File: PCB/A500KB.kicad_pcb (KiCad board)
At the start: 2 copper layers, 448.4 x 139.2 mm, 224 parts, among them J1 Conn_01x31, J2 USB_B, J3 Conn_02x03_Odd_Even, J4 Conn_01x08_Male, J5 Conn_01x02, Q1 MMBT3904, U1 IS32FL3237_DS, U2 AT90USB1287-AU, Y2 16 MHz

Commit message: added Spacebar holder for extra springs, adjusted PCB
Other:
- board size 448.4 x 139.2 mm -> 447.8 x 139.2 mm

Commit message: PCB update, Amiga software update  - finished intended feature set for Amiga    software: auto-load from keyboard, some    status and error requesters, automatic    custom screen if there are not enough    available pens on Workbench
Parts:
- D10, D11, D12, D13, D14, D15, D16, D17, D18, D19, D20, D21, D22, D23, D24, D25, D26, D27, D28, D29, D30, D31, D32, D33, D34, D35, D36, D37, D38, D39, D40, D41, D42, D43, D44, D45, D46, D47, D48, D49, D50, D54, D55, D56, D57, D58, D59, D60, D61, D62, D63, D64, D65, D66, D67, D68, D8, D9: value 1N914WT -> 1N4148W; footprint Diode_SMD:D_SOD-523 -> Diode_SMD:D_SOD-123
- moved D54 1.31 mm to (54.6, 267.5), turned to 270 degrees
- moved D36 1.25 mm to (296.8, 305.8), turned to 270 degrees
- moved D20 1.19 mm to (387.8, 324.6), turned to 270 degrees
- moved D34 1.16 mm to (258.8, 305.7), turned to 270 degrees
- moved D28 1.16 mm to (144.3, 305.7), turned to 270 degrees
- moved D29 1.16 mm to (163.4, 305.7), turned to 270 degrees
- moved D31 1.16 mm to (201.5, 305.7), turned to 270 degrees
- moved D33 1.16 mm to (239.7, 305.7), turned to 270 degrees
- moved D35 1.16 mm to (277.8, 305.7), turned to 270 degrees
- moved D27 1.16 mm to (125.3, 305.7), turned to 270 degrees
- moved D26 1.15 mm to (106.2, 305.7), turned to 270 degrees
- moved D30 1.15 mm to (182.4, 305.7), turned to 270 degrees
- moved D25 1.15 mm to (87.1, 305.7), turned to 270 degrees
- moved D32 1.15 mm to (220.6, 305.7), turned to 270 degrees
- moved D9 1.12 mm to (96.6, 324.6), turned to 270 degrees
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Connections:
- D10 pad 1: Net-(D10-Pad1) -> /X6=3
- D10 pad 2: /X6=3 -> Net-(D10-Pad2)
- D11 pad 1: Net-(D11-Pad1) -> /X6=3
- D11 pad 2: /X6=3 -> Net-(D11-Pad2)
- D12 pad 1: Net-(D12-Pad1) -> /X6=3
- D12 pad 2: /X6=3 -> Net-(D12-Pad2)
- D13 pad 1: Net-(D13-Pad1) -> /X6=3
- D13 pad 2: /X6=3 -> Net-(D13-Pad2)
- D14 pad 1: Net-(D14-Pad1) -> /X6=3
- D14 pad 2: /X6=3 -> Net-(D14-Pad2)
- D15 pad 1: Net-(D15-Pad1) -> /X6=3
- D15 pad 2: /X6=3 -> Net-(D15-Pad2)
- D16 pad 1: Net-(D16-Pad1) -> /X6=3
- D16 pad 2: /X6=3 -> Net-(D16-Pad2)
- D17 pad 1: Net-(D17-Pad1) -> /X6=3
- D17 pad 2: /X6=3 -> Net-(D17-Pad2)
- D18 pad 1: Net-(D18-Pad1) -> /X6=3
- D18 pad 2: /X6=3 -> Net-(D18-Pad2)
- D19 pad 1: Net-(D19-Pad1) -> /X6=3
- D19 pad 2: /X6=3 -> Net-(D19-Pad2)
- D20 pad 1: Net-(D20-Pad1) -> /X5=2
- D20 pad 2: /X5=2 -> Net-(D20-Pad2)
- D21 pad 1: Net-(D21-Pad1) -> /X4=1
- D21 pad 2: /X4=1 -> Net-(D21-Pad2)
- D22 pad 1: Net-(D22-Pad1) -> /X3=5
- D22 pad 2: /X3=5 -> Net-(D22-Pad2)
- D23 pad 1: Net-(D23-Pad1) -> /X6=3
- D23 pad 2: /X6=3 -> Net-(D23-Pad2)
- D24 pad 1: Net-(D24-Pad1) -> /X5=2
- D24 pad 2: /X5=2 -> Net-(D24-Pad2)
- D25 pad 1: Net-(D25-Pad1) -> /X5=2
- D25 pad 2: /X5=2 -> Net-(D25-Pad2)
- D26 pad 1: Net-(D26-Pad1) -> /X5=2
- D26 pad 2: /X5=2 -> Net-(D26-Pad2)
- D27 pad 1: Net-(D27-Pad1) -> /X5=2
- D27 pad 2: /X5=2 -> Net-(D27-Pad2)
- D28 pad 1: Net-(D28-Pad1) -> /X5=2
- D28 pad 2: /X5=2 -> Net-(D28-Pad2)
- D29 pad 1: Net-(D29-Pad1) -> /X5=2
- D29 pad 2: /X5=2 -> Net-(D29-Pad2)
- D30 pad 1: Net-(D30-Pad1) -> /X5=2
- D30 pad 2: /X5=2 -> Net-(D30-Pad2)
- D31 pad 1: Net-(D31-Pad1) -> /X5=2
- D31 pad 2: /X5=2 -> Net-(D31-Pad2)
- D32 pad 1: Net-(D32-Pad1) -> /X5=2
- D32 pad 2: /X5=2 -> Net-(D32-Pad2)
- D33 pad 1: Net-(D33-Pad1) -> /X5=2
- D33 pad 2: /X5=2 -> Net-(D33-Pad2)
- D34 pad 1: Net-(D34-Pad1) -> /X5=2
- D34 pad 2: /X5=2 -> Net-(D34-Pad2)
- D35 pad 1: Net-(D35-Pad1) -> /X5=2
- D35 pad 2: /X5=2 -> Net-(D35-Pad2)
- D36 pad 1: Net-(D36-Pad1) -> /X5=2
- D36 pad 2: /X5=2 -> Net-(D36-Pad2)
- D37 pad 1: Net-(D37-Pad1) -> /X4=1
- D37 pad 2: /X4=1 -> Net-(D37-Pad2)
- D38 pad 1: Net-(D38-Pad1) -> /X4=1
- D38 pad 2: /X4=1 -> Net-(D38-Pad2)
- D39 pad 1: Net-(D39-Pad1) -> /X4=1
- D39 pad 2: /X4=1 -> Net-(D39-Pad2)
- D40 pad 1: Net-(D40-Pad1) -> /X4=1
- D40 pad 2: /X4=1 -> Net-(D40-Pad2)
- D41 pad 1: Net-(D41-Pad1) -> /X4=1
- D41 pad 2: /X4=1 -> Net-(D41-Pad2)
- D42 pad 1: Net-(D42-Pad1) -> /X4=1
- D42 pad 2: /X4=1 -> Net-(D42-Pad2)
- D43 pad 1: Net-(D43-Pad1) -> /X4=1
- D43 pad 2: /X4=1 -> Net-(D43-Pad2)
- D44 pad 1: Net-(D44-Pad1) -> /X4=1
- D44 pad 2: /X4=1 -> Net-(D44-Pad2)
- D45 pad 1: Net-(D45-Pad1) -> /X4=1
- D45 pad 2: /X4=1 -> Net-(D45-Pad2)
- D46 pad 1: Net-(D46-Pad1) -> /X4=1
- D46 pad 2: /X4=1 -> Net-(D46-Pad2)
- D47 pad 1: Net-(D47-Pad1) -> /X4=1
- D47 pad 2: /X4=1 -> Net-(D47-Pad2)
- D48 pad 1: Net-(D48-Pad1) -> /X4=1
- D48 pad 2: /X4=1 -> Net-(D48-Pad2)
- D49 pad 1: Net-(D49-Pad1) -> /X4=1
- D49 pad 2: /X4=1 -> Net-(D49-Pad2)
- D50 pad 1: Net-(D50-Pad1) -> /X4=1
- D50 pad 2: /X4=1 -> Net-(D50-Pad2)
- D54 pad 1: Net-(D54-Pad1) -> /X3=5
- D54 pad 2: /X3=5 -> Net-(D54-Pad2)
- D55 pad 1: Net-(D55-Pad1) -> /X3=5
- D55 pad 2: /X3=5 -> Net-(D55-Pad2)
- D56 pad 1: Net-(D56-Pad1) -> /X3=5
- D56 pad 2: /X3=5 -> Net-(D56-Pad2)
- D57 pad 1: Net-(D57-Pad1) -> /X3=5
- D57 pad 2: /X3=5 -> Net-(D57-Pad2)
- D58 pad 1: Net-(D58-Pad1) -> /X3=5
- D58 pad 2: /X3=5 -> Net-(D58-Pad2)
- D59 pad 1: Net-(D59-Pad1) -> /X3=5
- D59 pad 2: /X3=5 -> Net-(D59-Pad2)
- D60 pad 1: Net-(D60-Pad1) -> /X3=5
- D60 pad 2: /X3=5 -> Net-(D60-Pad2)
- D61 pad 1: Net-(D61-Pad1) -> /X3=5
- D61 pad 2: /X3=5 -> Net-(D61-Pad2)
- D62 pad 1: Net-(D62-Pad1) -> /X3=5
- D62 pad 2: /X3=5 -> Net-(D62-Pad2)
- D63 pad 1: Net-(D63-Pad1) -> /X3=5
- D63 pad 2: /X3=5 -> Net-(D63-Pad2)
- D64 pad 1: Net-(D64-Pad1) -> /X3=5
- D64 pad 2: /X3=5 -> Net-(D64-Pad2)
- D65 pad 1: Net-(D65-Pad1) -> /X3=5
- D65 pad 2: /X3=5 -> Net-(D65-Pad2)
- D66 pad 1: Net-(D66-Pad1) -> /X3=5
- D66 pad 2: /X3=5 -> Net-(D66-Pad2)
- D67 pad 1: Net-(D67-Pad1) -> /X3=5
- D67 pad 2: /X3=5 -> Net-(D67-Pad2)
- D68 pad 1: Net-(D68-Pad1) -> /X6=3
- D68 pad 2: /X6=3 -> Net-(D68-Pad2)
- D8 pad 1: Net-(D8-Pad1) -> /X6=3
- D8 pad 2: /X6=3 -> Net-(D8-Pad2)
- D9 pad 1: Net-(D9-Pad1) -> /X6=3
- D9 pad 2: /X6=3 -> Net-(D9-Pad2)
- MX10 pad 2: Net-(D24-Pad1) -> Net-(D24-Pad2)
- MX11 pad 2: Net-(D8-Pad1) -> Net-(D8-Pad2)
- MX14 pad 2: Net-(D56-Pad1) -> Net-(D56-Pad2)
- MX15 pad 2: Net-(D39-Pad1) -> Net-(D39-Pad2)
- MX16 pad 2: Net-(D25-Pad1) -> Net-(D25-Pad2)
- MX17 pad 2: Net-(D9-Pad1) -> Net-(D9-Pad2)
- MX19 pad 2: Net-(D57-Pad1) -> Net-(D57-Pad2)
- MX2 pad 2: Net-(D54-Pad1) -> Net-(D54-Pad2)
- MX20 pad 2: Net-(D40-Pad1) -> Net-(D40-Pad2)
- MX21 pad 2: Net-(D26-Pad1) -> Net-(D26-Pad2)
- MX22 pad 2: Net-(D10-Pad1) -> Net-(D10-Pad2)
- MX24 pad 2: Net-(D58-Pad1) -> Net-(D58-Pad2)
- MX25 pad 2: Net-(D41-Pad1) -> Net-(D41-Pad2)
- MX26 pad 2: Net-(D27-Pad1) -> Net-(D27-Pad2)
- MX27 pad 2: Net-(D11-Pad1) -> Net-(D11-Pad2)
- MX29 pad 2: Net-(D59-Pad1) -> Net-(D59-Pad2)
- MX3 pad 2: Net-(D37-Pad1) -> Net-(D37-Pad2)
- MX30 pad 2: Net-(D42-Pad1) -> Net-(D42-Pad2)
- MX31 pad 2: Net-(D28-Pad1) -> Net-(D28-Pad2)
- MX32 pad 2: Net-(D12-Pad1) -> Net-(D12-Pad2)
- MX33 pad 2: Net-(D13-Pad1) -> Net-(D13-Pad2)
- MX35 pad 2: Net-(D60-Pad1) -> Net-(D60-Pad2)
- MX36 pad 2: Net-(D43-Pad1) -> Net-(D43-Pad2)
- MX37 pad 2: Net-(D29-Pad1) -> Net-(D29-Pad2)
- MX38 pad 2: Net-(D14-Pad1) -> Net-(D14-Pad2)
- MX40 pad 2: Net-(D61-Pad1) -> Net-(D61-Pad2)
- MX41 pad 2: Net-(D44-Pad1) -> Net-(D44-Pad2)
- MX42 pad 2: Net-(D30-Pad1) -> Net-(D30-Pad2)
- MX43 pad 2: Net-(D15-Pad1) -> Net-(D15-Pad2)
- MX45 pad 2: Net-(D62-Pad1) -> Net-(D62-Pad2)
- MX46 pad 2: Net-(D45-Pad1) -> Net-(D45-Pad2)
- MX47 pad 2: Net-(D31-Pad1) -> Net-(D31-Pad2)
- MX48 pad 2: Net-(D16-Pad1) -> Net-(D16-Pad2)
- MX50 pad 2: Net-(D63-Pad1) -> Net-(D63-Pad2)
- MX51 pad 2: Net-(D46-Pad1) -> Net-(D46-Pad2)
- MX52 pad 2: Net-(D32-Pad1) -> Net-(D32-Pad2)
- MX53 pad 2: Net-(D17-Pad1) -> Net-(D17-Pad2)
- MX55 pad 2: Net-(D64-Pad1) -> Net-(D64-Pad2)
- MX56 pad 2: Net-(D47-Pad1) -> Net-(D47-Pad2)
- MX57 pad 2: Net-(D33-Pad1) -> Net-(D33-Pad2)
- MX58 pad 2: Net-(D18-Pad1) -> Net-(D18-Pad2)
- MX60 pad 2: Net-(D65-Pad1) -> Net-(D65-Pad2)
- MX61 pad 2: Net-(D48-Pad1) -> Net-(D48-Pad2)
- MX62 pad 2: Net-(D34-Pad1) -> Net-(D34-Pad2)
- MX63 pad 2: Net-(D19-Pad1) -> Net-(D19-Pad2)
- MX65 pad 2: Net-(D66-Pad1) -> Net-(D66-Pad2)
- MX66 pad 2: Net-(D49-Pad1) -> Net-(D49-Pad2)
- MX67 pad 2: Net-(D35-Pad1) -> Net-(D35-Pad2)
- MX69 pad 2: Net-(D67-Pad1) -> Net-(D67-Pad2)
- MX70 pad 2: Net-(D36-Pad1) -> Net-(D36-Pad2)
- MX71 pad 2: Net-(D50-Pad1) -> Net-(D50-Pad2)
- MX72 pad 2: Net-(D68-Pad1) -> Net-(D68-Pad2)
- MX74 pad 2: Net-(D21-Pad1) -> Net-(D21-Pad2)
- MX75 pad 2: Net-(D22-Pad1) -> Net-(D22-Pad2)
- MX76 pad 2: Net-(D23-Pad1) -> Net-(D23-Pad2)
- MX78 pad 2: Net-(D20-Pad1) -> Net-(D20-Pad2)
- MX8 pad 2: Net-(D55-Pad1) -> Net-(D55-Pad2)
- MX9 pad 2: Net-(D38-Pad1) -> Net-(D38-Pad2)
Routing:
- net GND: track 1080.6 -> 887.7 mm, vias 150 -> 148
- net Net-(D13-Pad1): track 18.4 -> 0.00 mm
- net Net-(D37-Pad1): track 17.0 -> 0.00 mm
- net Net-(D13-Pad2): track 0.00 -> 16.6 mm
- net Net-(D37-Pad2): track 0.00 -> 16.1 mm
- net Net-(D54-Pad1): track 12.2 -> 0.00 mm
- net Net-(D50-Pad2): track 0.00 -> 12.2 mm
- net Net-(D54-Pad2): track 0.00 -> 12.1 mm
- net Net-(D50-Pad1): track 11.1 -> 0.00 mm
- net Net-(D24-Pad2): track 0.00 -> 10.4 mm
- net Net-(D24-Pad1): track 9.81 -> 0.00 mm
- net Net-(D68-Pad1): track 7.71 -> 0.00 mm
- net Net-(D67-Pad1): track 7.65 -> 0.00 mm
- net Net-(D20-Pad2): track 0.00 -> 7.61 mm
- net Net-(D21-Pad1): track 7.56 -> 0.00 mm
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
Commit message: Some more adjustments to Footprints, updated doc
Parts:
- added REF**: baxlogo, Bax:baxlogo, F.Cu at (462.2, 228.8)
- J2: value USB_B -> USB_B_Micro; footprint Connector_USB:USB_B_Lumberg_2411_02_Horizontal -> Connector_USB:USB_Micro-B_Molex-105017-0001
- R13, R14: value 2k -> 3.3k
- moved J2 13.1 mm to (319.9, 225.4), turned to 180 degrees
- moved R3 8.44 mm to (318.7, 234.9)
- moved R4 8.41 mm to (321.1, 234.9)
- moved H10 0.45 mm to (471.2, 284.3)
- moved H11 0.45 mm to (471.2, 303.2)
- moved H12 0.45 mm to (471.2, 322.4)
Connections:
- J2 pad 4: GND -> Net-(J2-Pad4)
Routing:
- net +5V: track 817.5 -> 835.5 mm
- net /LSHIFT: track 401.1 -> 415.5 mm
- net GND: track 887.7 -> 899.2 mm, vias 148 -> 159
- net /Y1=28: track 347.6 -> 358.7 mm
- net /RSHFT: track 141.4 -> 151.5 mm
- net /D+: track 28.0 -> 22.8 mm
- net /D-: track 25.5 -> 20.3 mm
- net /Y2=27: track 456.6 -> 460.2 mm
- net /Y14=15: track 613.0 -> 616.5 mm
- net Net-(D13-Pad2): track 16.6 -> 20.0 mm
- net /X7=4: track 507.3 -> 509.5 mm
- net /CAPSR: track 448.4 -> 450.6 mm
- net /CAPSB: track 441.5 -> 443.8 mm
- net /D--: track 4.58 -> 6.81 mm
- net /CAPSG: track 443.9 -> 446.1 mm
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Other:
- board text added: "A500KB for Mitsumi or Cherry switches Rev.2 © 2021-22 Henryk Richter"
- board text removed: "A500KB for Mitsumi or Cherry switches © 2021 Henryk Richter"

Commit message: minor adjustments to main PCB
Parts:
- moved D24 0.40 mm to (68.8, 312.9)
- moved D2 0.33 mm to (68.8, 307.8), turned to 270 degrees
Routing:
- net /X7=4: track 509.5 -> 523.8 mm
- net /X2=7: track 571.4 -> 578.0 mm
- net /CAPSB: track 443.8 -> 447.9 mm
- net Net-(D13-Pad2): track 20.0 -> 22.9 mm
- net +5V: track 835.5 -> 838.2 mm
- net /CAPSR: track 450.6 -> 452.8 mm
- net /CAPSG: track 446.1 -> 448.0 mm
- net /Y2=27: track 460.2 -> 461.5 mm
- net CAPSLED: track 367.1 -> 365.7 mm
- net /Y1=28: track 358.7 -> 359.9 mm
- net /X5=2: track 502.0 -> 502.9 mm
- net MOSI: track 228.3 -> 228.9 mm
- net Net-(D24-Pad2): track 10.4 -> 10.9 mm
- net GND: vias 159 -> 161
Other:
- outline, holes or cut-outs redrawn
- board text added: "o"

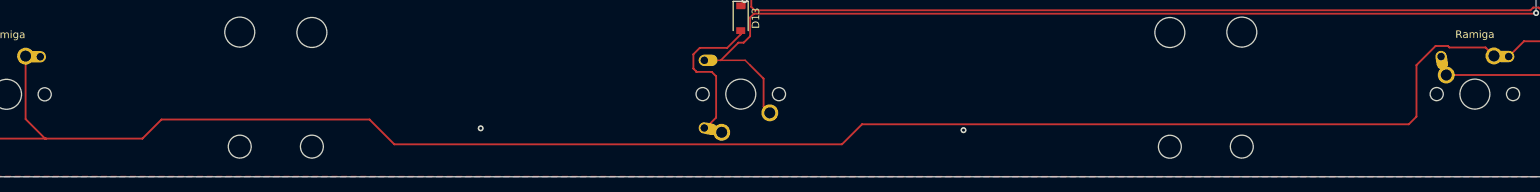
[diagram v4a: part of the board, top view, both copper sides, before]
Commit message: finalized V2 design, LED defaults include IN4 now
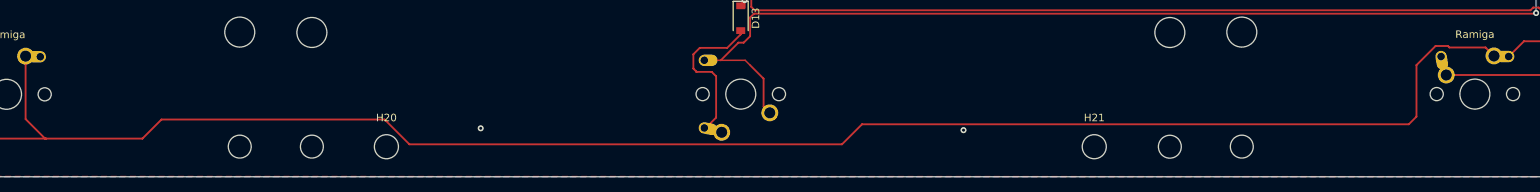
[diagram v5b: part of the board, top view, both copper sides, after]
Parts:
- added H20: MountingHole, MXMitsumi:MountingHole_3.2mm_M3_Small_Bax, F.Cu at (126.5, 357.9)
- added H21: MountingHole, MXMitsumi:MountingHole_3.2mm_M3_Small_Bax, F.Cu at (220.7, 357.9)

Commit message: PCB update  - marked some unneeded components N/A  - changed LED footprints to fit PLCC LEDs better  - moved A500KBMini connector 0.5mm downwards
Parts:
- moved D3 0.06 mm to (456.9, 243.4)
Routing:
- net +5V: track 838.2 -> 840.7 mm
- net /F1G: track 18.0 -> 19.8 mm, vias 0 -> 2
- net /CAPSR: track 452.8 -> 454.4 mm
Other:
- board text added: "A"
- board text added: "B"
- board text added: "G"
- board text added: "R"
